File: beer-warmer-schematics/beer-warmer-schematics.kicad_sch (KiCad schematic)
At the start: 31 parts, among them J1 USB_C_Receptacle_USB2.0_14P, J2 Screw_Terminal_01x02, J3 Conn_01x07_Socket, J4 Conn_01x07_Socket, J5 Conn_01x04_Pin, J6 Screw_Terminal_01x03, Q1 AOD4184A, U2 LM2596S-5, U3 CH224K

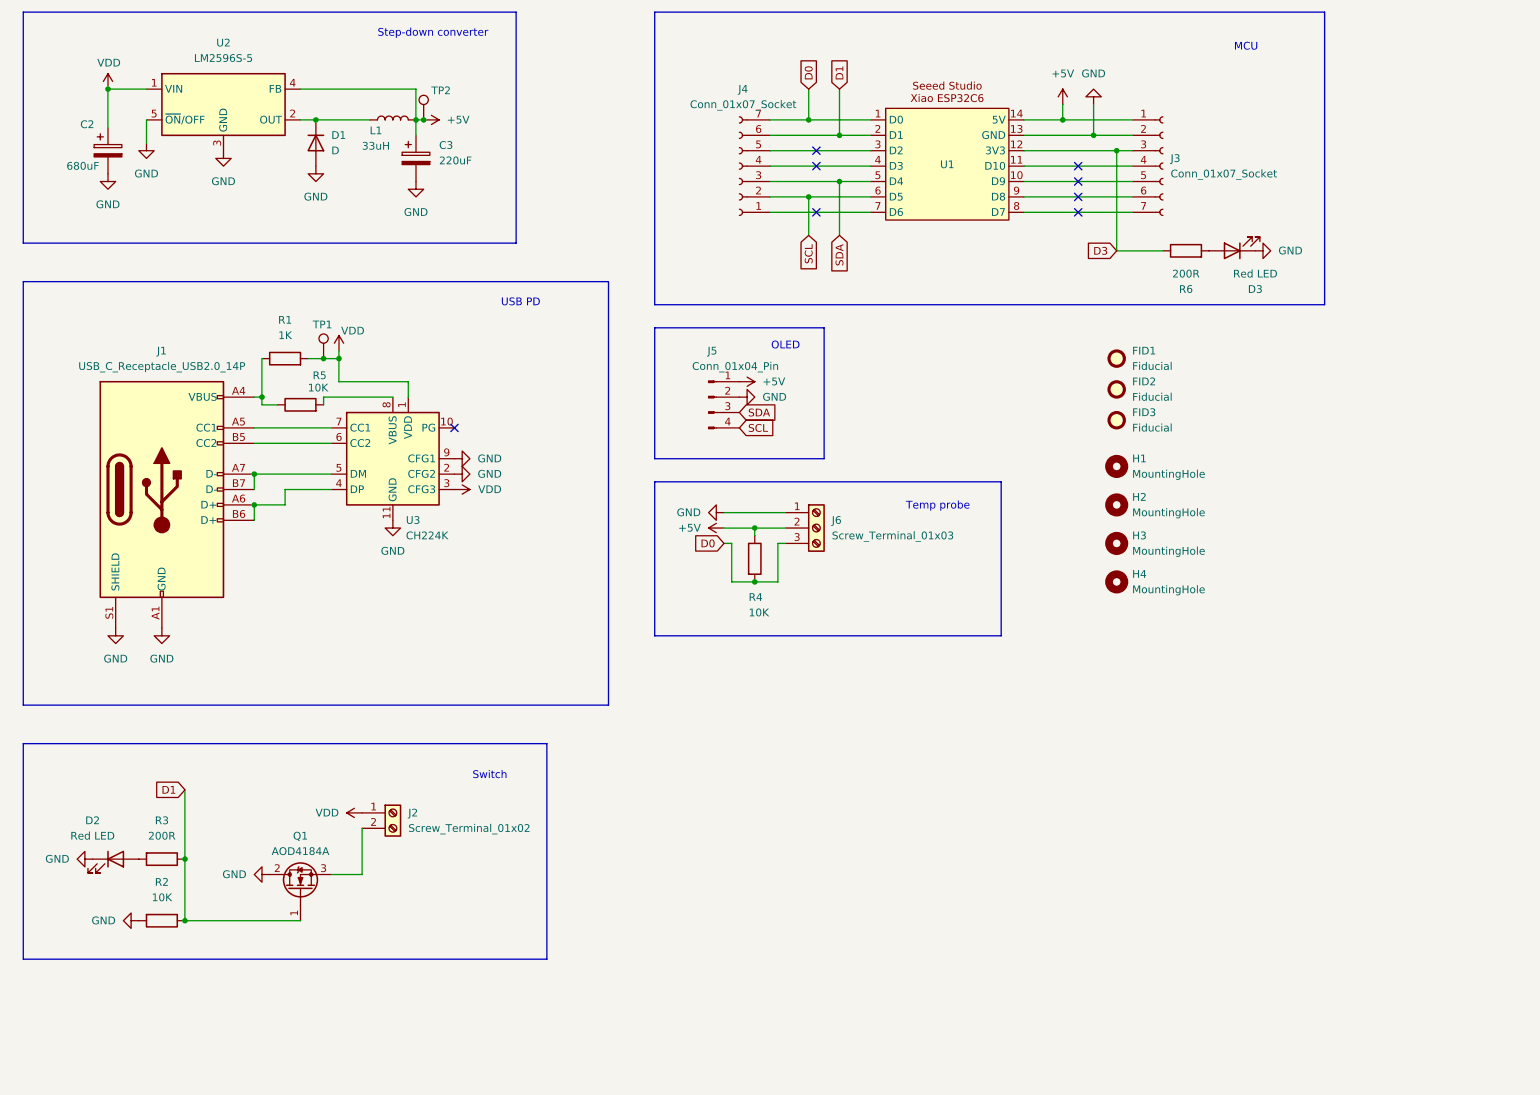
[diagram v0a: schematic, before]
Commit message: fix a bunch of potential issues, add current sense
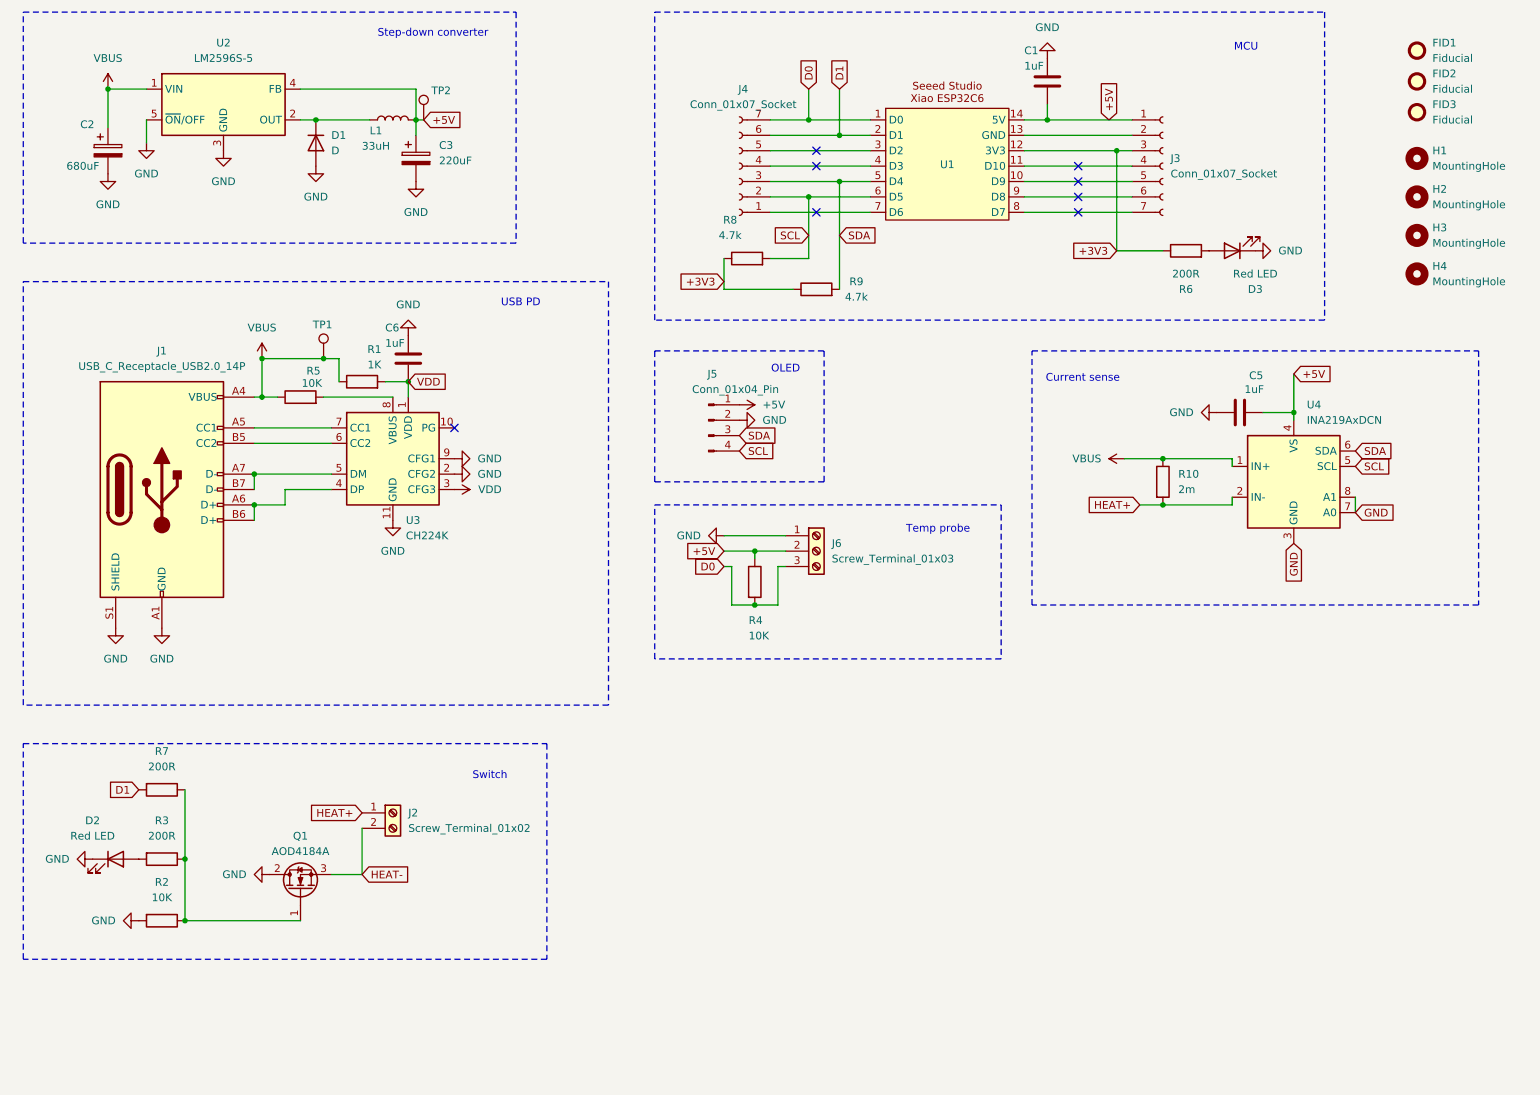
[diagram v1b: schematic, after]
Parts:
- added C1, C5, C6: 1uF, Capacitor_SMD:C_0402_1005Metric, symbol Device:C
- added R10: 2m, Resistor_SMD:R_1206_3216Metric, symbol Device:R
- added R7: 200R, Resistor_SMD:R_0603_1608Metric, symbol Device:R
- added R8, R9: 4.7k, Resistor_SMD:R_0603_1608Metric, symbol Device:R
- added U4: INA219AxDCN, Package_TO_SOT_SMD:SOT-23-8, symbol Sensor_Energy:INA219AxDCN
- R1: footprint Resistor_SMD:R_1206_3216Metric -> Resistor_SMD:R_0603_1608Metric; LCSC C4410 -> C21190
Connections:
- net +5V: now also C1.2, C5.1, U4.4 (VS)
- net D1: now also R7.2; no longer Q1.1 (G), R2.1, R3.1
- net GND: now also C1.1, C5.2, C6.1, U4.3 (GND), U4.7 (A0), U4.8 (A1); no longer J3.2 (Pin_2), U1.13 (GND)
- net SCL: now also R8.2, U4.5 (SCL)
- net SDA: now also R9.2, U4.6 (SDA)
- net VDD: now also C6.2; no longer C2.1, J2.1 (Pin_1), TP1.1, U2.1 (VIN)
- net VBUS: now reaches J1.A4 (VBUS), J1.A9 (VBUS), J1.B4 (VBUS), J1.B9 (VBUS), R1.1, R5.1
- net VBUS: now also C2.1, TP1.1, U2.1 (VIN), R10.1, U4.1 (IN+)
- net HEAT-: now reaches J2.2 (Pin_2), Q1.3 (S)
- net D3 renamed +3V3
- net +3V3: now also R8.1, R9.1
- new net: Q1.1 (G), R2.1, R3.1, R7.1
- new net: J3.2 (Pin_2), U1.13 (GND)
- new net HEAT+: J2.1 (Pin_1), R10.2, U4.2 (IN-)
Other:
- note added: "Current sense"
- moved on the sheet: FID1, FID2, FID3, H1, H2, H3, H4, J5, J6, R1, R4, R5

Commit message: middle ground plane, 12v over dedicated tracks to avoid noise
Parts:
- R10: value 2m -> 20m; LCSC C2937385 -> C393094
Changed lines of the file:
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@@
 			)
 		)
-		(property "Value" "2m"
+		(property "Value" "20m"
 			(at 218.44 96.5199 0)
 			(effects
@@
 			)
 		)
-		(property "LCSC" "C2937385"
+		(property "LCSC" "C393094"
 			(at 215.9 95.25 0)
 			(effects

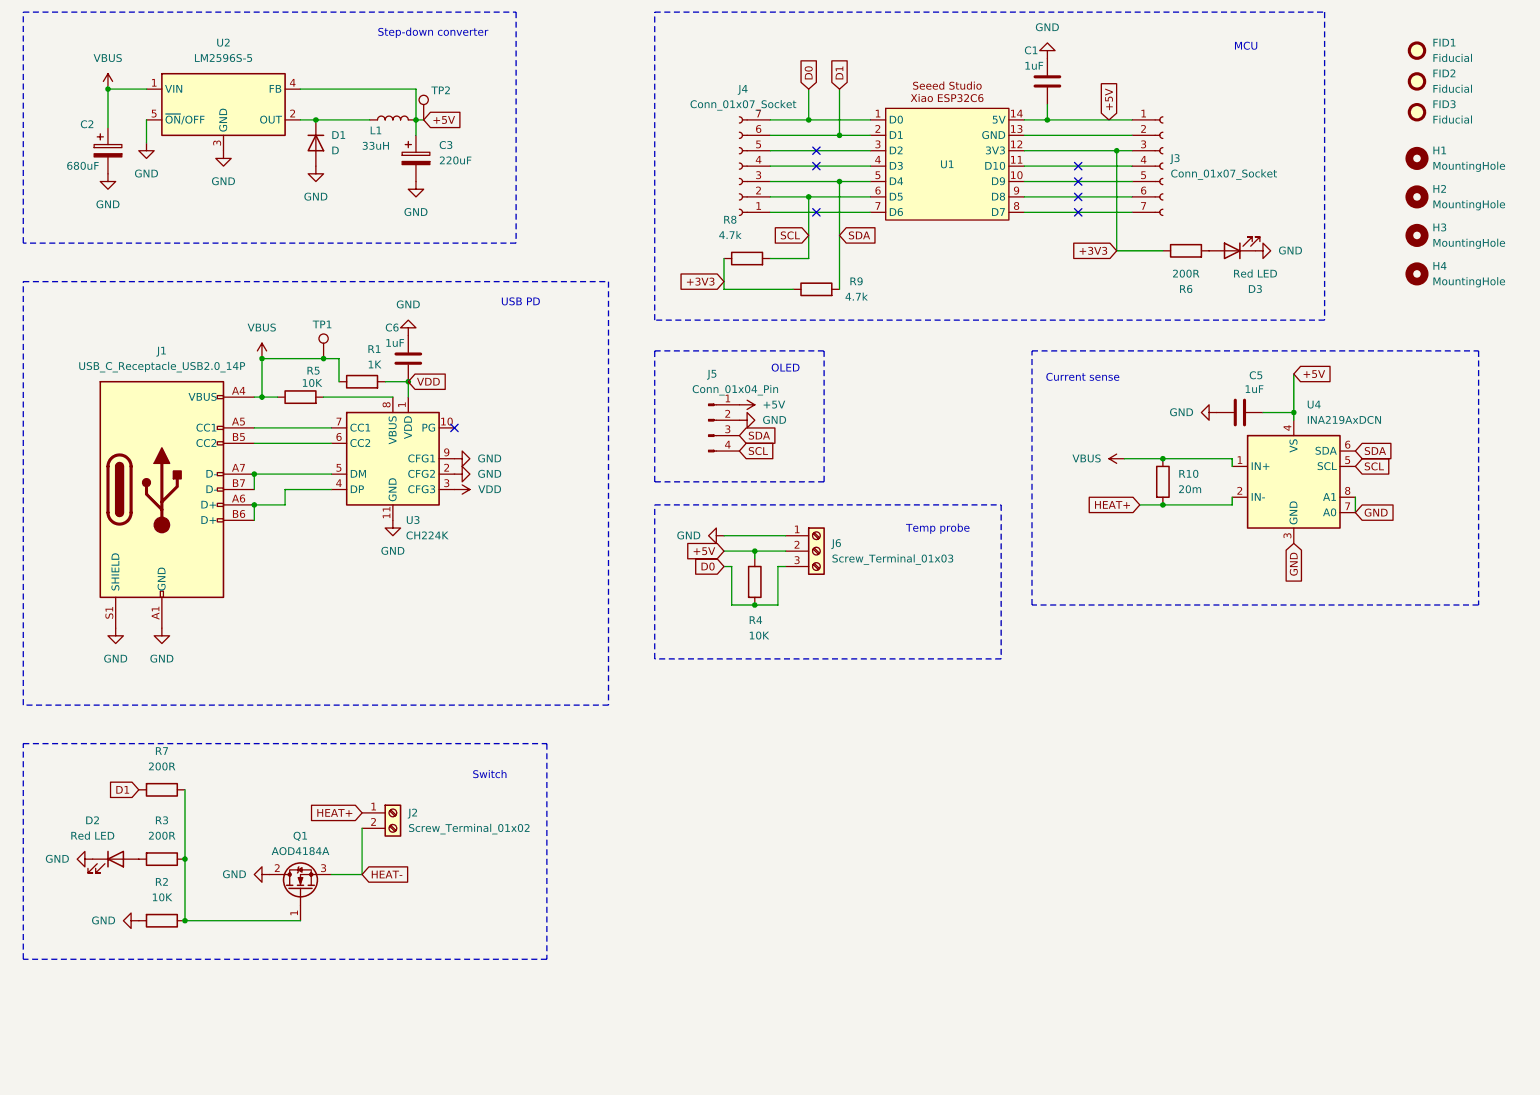
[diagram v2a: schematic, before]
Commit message: clean up schematics, correct mosfet orientation
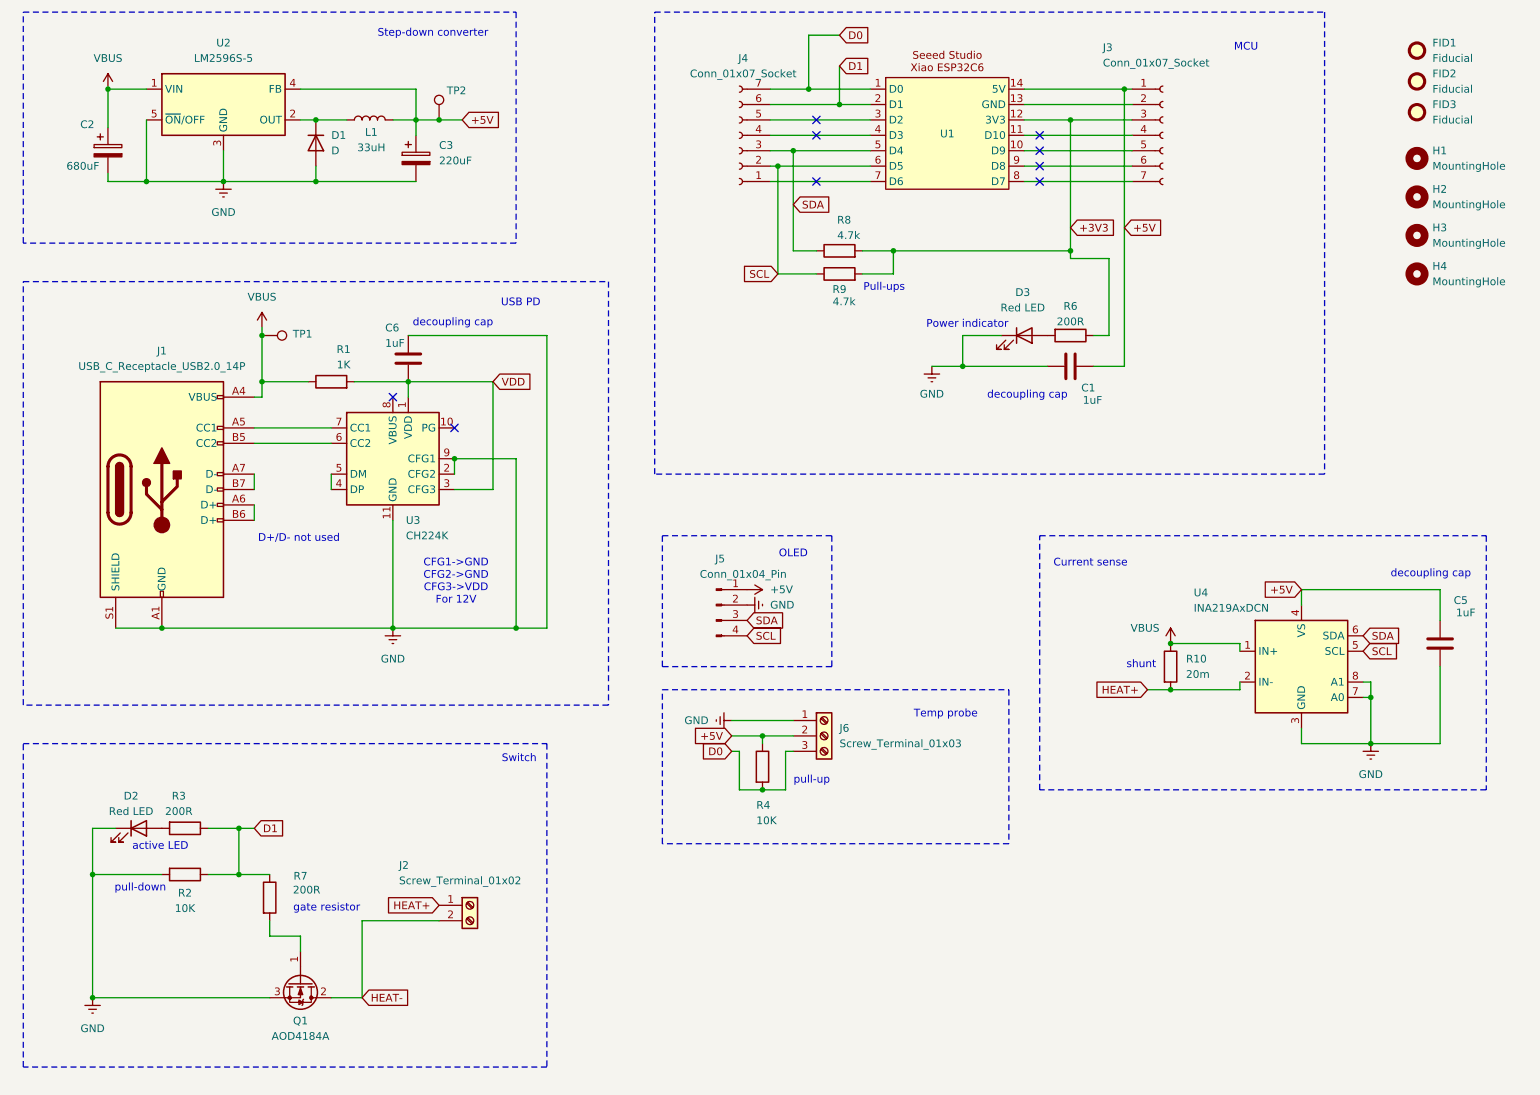
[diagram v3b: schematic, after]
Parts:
- removed R5: 10K, Resistor_SMD:R_0603_1608Metric, symbol Device:R
- J1: footprint Library:USB_C_Receptacle_Molex_105450-0101 -> Connector_USB:USB_C_Receptacle_GCT_USB4125-xx-x_6P_TopMnt_Horizontal; LCSC C134092 -> C456012
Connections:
- net +3V3: now also R8.2, R9.2; no longer R8.1, R9.1
- net +5V: now also C1.1, C5.2; no longer C1.2, C5.1
- net D1: now also R2.1, R3.1, R7.1; no longer R7.2
- net GND: now also C1.2, C5.1, Q1.3 (S); no longer C1.1, C5.2, Q1.2 (D)
- net HEAT-: now also Q1.2 (D); no longer Q1.3 (S)
- net SCL: now also R9.1; no longer R8.2
- net SDA: now also R8.1; no longer R9.2
- net at J1.A6 (D+), J1.B6 (D+): no longer U3.4 (DP)
- net at J1.A7 (D-), J1.B7 (D-): no longer U3.5 (DM)
- new net: Q1.1 (G), R7.2
- new net: U3.4 (DP), U3.5 (DM)
- no-connect marks 8 -> 9
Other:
- note added: "CFG1->GND CFG2->GND CFG3->VDD For 12V"
- note added: "D+/D- not used"
- note added: "Power indicator"
- note added: "Pull-ups"
- note added: "active LED"
- note added: "decoupling cap"
- note added: "gate resistor"
- note added: "pull-down"
- note added: "pull-up"
- note added: "shunt"
- moved on the sheet: C1, C5, D2, D3, J2, J3, J4, J5, J6, L1, Q1, R1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

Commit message: led indicator on vbus power
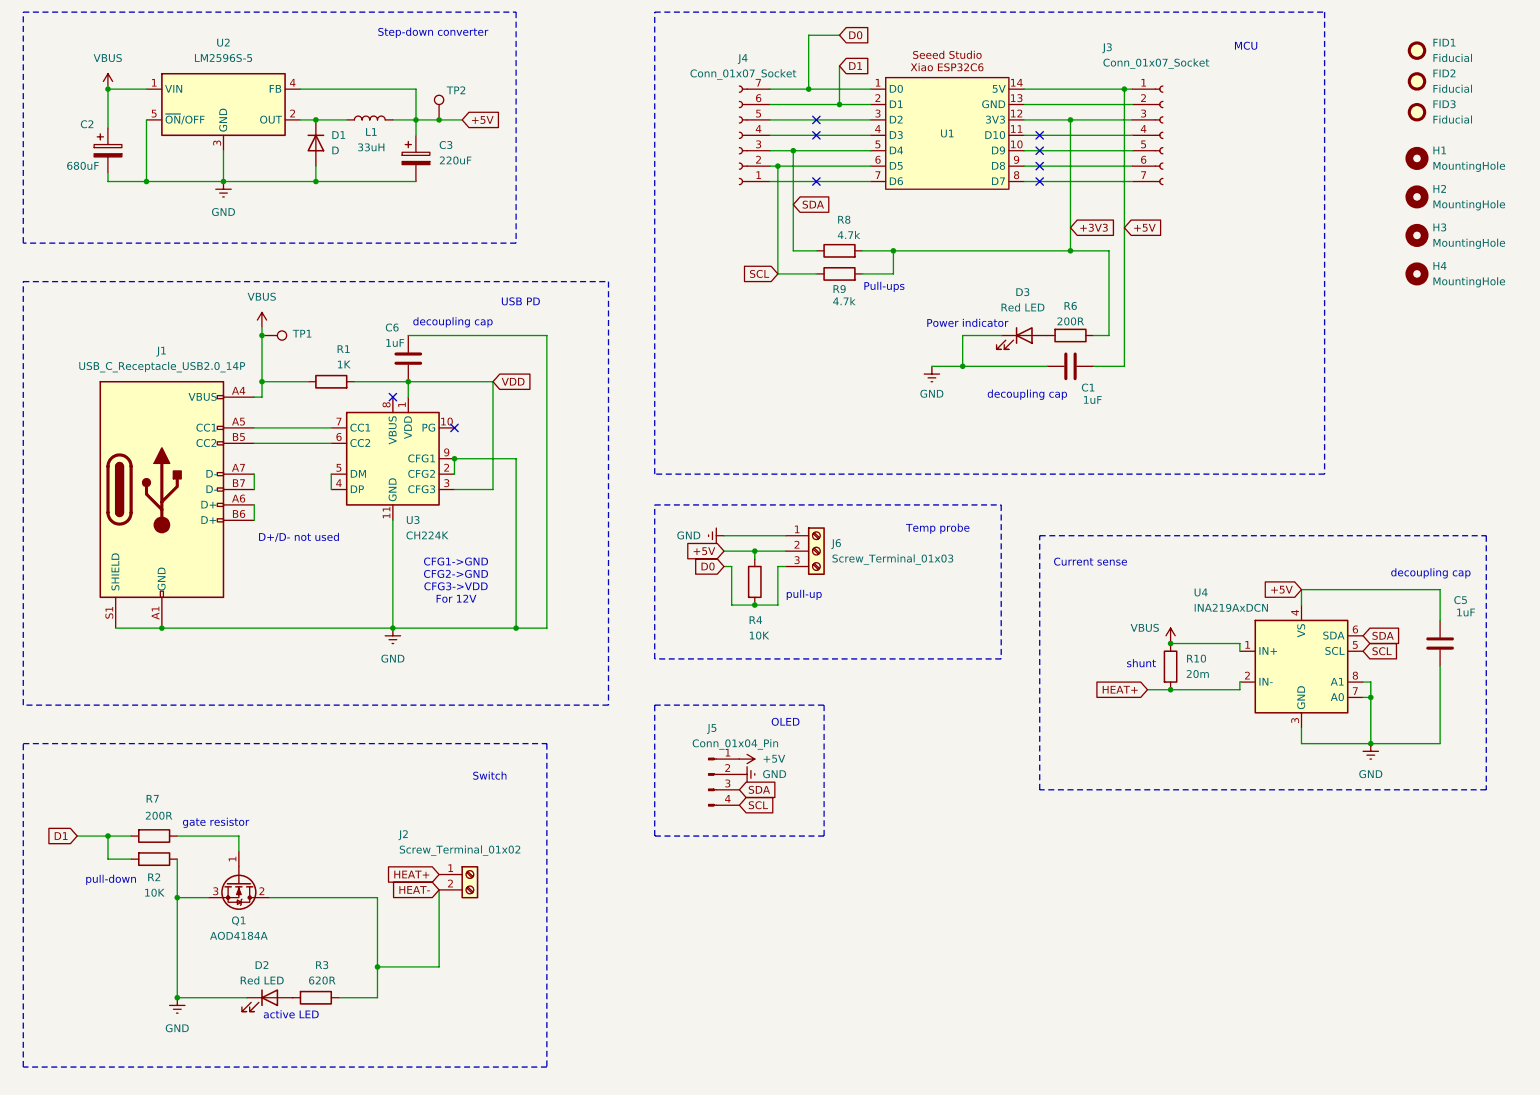
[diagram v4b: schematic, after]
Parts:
- R3: value 200R -> 620R; footprint Resistor_SMD:R_0603_1608Metric -> Resistor_SMD:R_1206_3216Metric; LCSC C22962 -> C25391
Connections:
- net D1: now also R2.2, R7.2; no longer R2.1, R3.1, R7.1
- net GND: now also R2.1; no longer R2.2
- net HEAT-: now also R3.1
- net at Q1.1 (G): now also R7.1; no longer R7.2
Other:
- moved on the sheet: D2, J2, J5, J6, Q1, R2, R3, R4, R7
